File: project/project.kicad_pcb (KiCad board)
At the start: 2 copper layers, 85.6 x 54 mm, 11 parts, among them U1 NT3H2211W0FTTJ

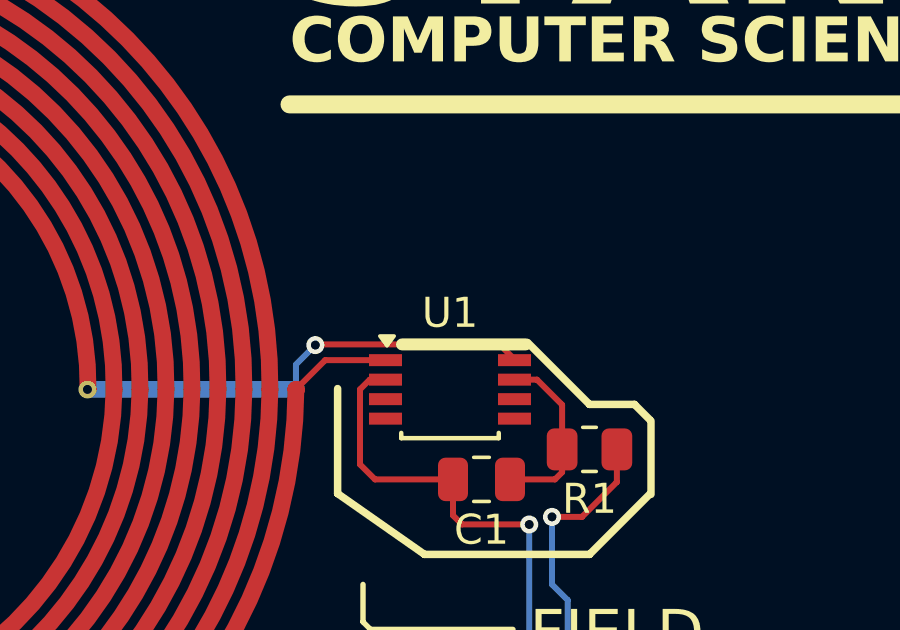
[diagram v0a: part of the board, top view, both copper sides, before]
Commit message: Restructured folder's files
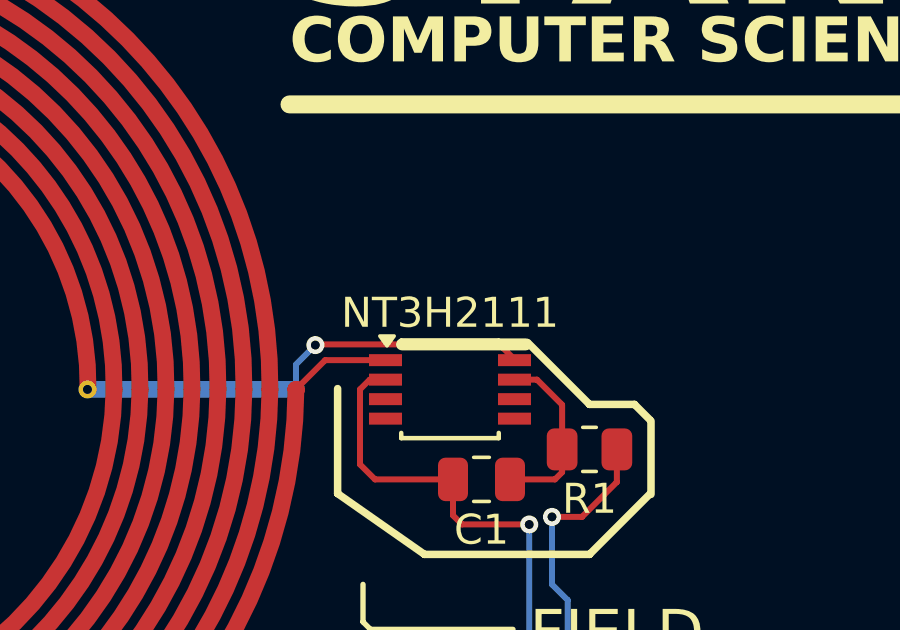
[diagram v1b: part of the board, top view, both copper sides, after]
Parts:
- removed U1: NT3H2211W0FTTJ, Package_SO:TSSOP-8_3x3mm_P0.65mm
- added NT3H2111: , Package_SO:TSSOP-8_3x3mm_P0.65mm, F.Cu at (157.8, 77.0)
